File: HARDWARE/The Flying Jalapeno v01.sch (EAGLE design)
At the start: 94 parts, among them J2 7V, Q1 16MHZ, Q3 P-Channel MOSFET, Q5 MOSFET-PCHANNELNDP6020P_20V_2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, Q6 200mA/50V, Q7 200mA/50V, U4 ATMEGA2560AU

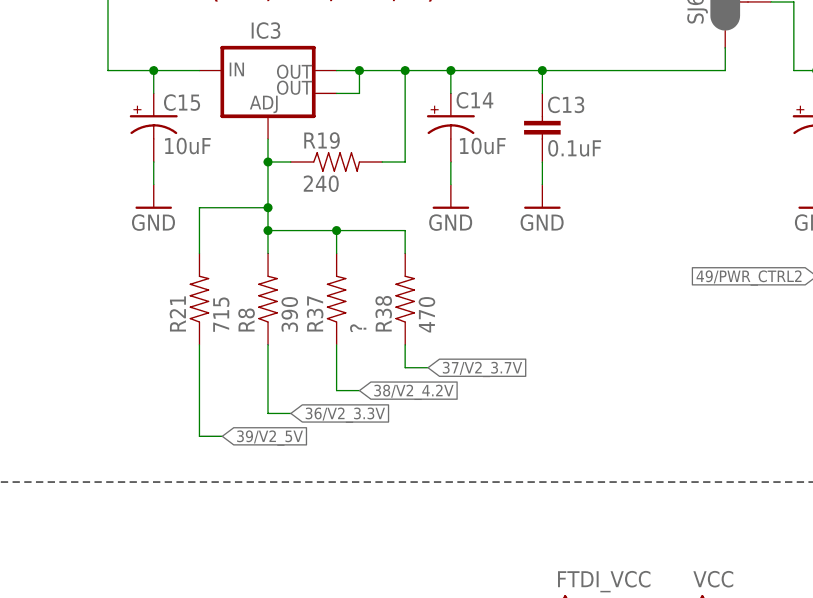
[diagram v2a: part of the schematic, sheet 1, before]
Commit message: finalized resistor values on lipo fake out vreg
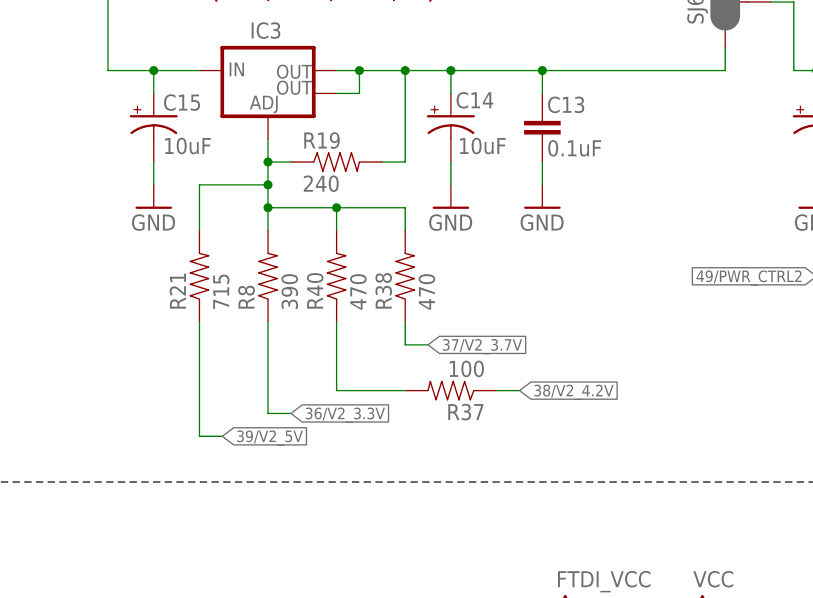
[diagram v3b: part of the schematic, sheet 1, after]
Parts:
- added R40: 470, SparkFun-Resistors:470OHM1/10W1%(0603)
- R37: value ? -> 100; device SparkFun-Resistors:390OHM1/10W1%(0603) -> SparkFun-Resistors:100OHM-1/10W-1%(0603)
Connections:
- new net N$1: R37.2, R40.1
- net N$10: now also R40.2; no longer R37.2
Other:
- moved on the sheet: R21, R37, R38, R8
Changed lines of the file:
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@@
 <part name="R36" library="SparkFun-Resistors" deviceset="10KOHM-1/10W-1%(0603)" device="0603" value="10K"/>
 <part name="GND38" library="SparkFun" deviceset="GND" device=""/>
-<part name="R37" library="SparkFun-Resistors" deviceset="390OHM1/10W1%(0603)" device="" value="?"/>
+<part name="R37" library="SparkFun-Resistors" deviceset="100OHM-1/10W-1%(0603)" device="" value="100"/>
 <part name="R38" library="SparkFun-Resistors" deviceset="470OHM1/10W1%(0603)" device="" value="470"/>
 <part name="R39" library="SparkFun-Resistors" deviceset="100KOHM-1/10W-1%(0603)" device="" value="100k"/>
@@
 <part name="R34" library="SparkFun-Resistors" deviceset="10KOHM-1/10W-1%(0603)" device="0603" value="10K"/>
 <part name="R35" library="SparkFun-Resistors" deviceset="10KOHM-1/10W-1%(0603)" device="0603" value="10K"/>
+<part name="R40" library="SparkFun-Resistors" deviceset="470OHM1/10W1%(0603)" device="" value="470"/>
 </parts>
 <sheets>
@@
 <attribute name="VALUE" x="71.12" y="121.92" size="1.778" layer="96"/>
 </instance>
-<instance part="R8" gate="G$1" x="68.58" y="106.68" rot="R90"/>
+<instance part="R8" gate="G$1" x="68.58" y="109.22" rot="R90"/>
 <instance part="R19" gate="G$1" x="76.2" y="121.92"/>
 <instance part="GND30" gate="1" x="99.06" y="116.84"/>
@@
 <attribute name="VALUE" x="165.608" y="122.174" size="1.778" layer="96" rot="R90"/>
 </instance>
-<instance part="R21" gate="G$1" x="60.96" y="106.68" rot="R90"/>
+<instance part="R21" gate="G$1" x="60.96" y="109.22" rot="R90"/>
 <instance part="SJ5" gate="G$1" x="114.3" y="203.2" smashed="yes" rot="MR0">
 <attribute name="NAME" x="110.109" y="200.66" size="1.778" layer="95" rot="MR90"/>
@@
 <instance part="R36" gate="G$1" x="149.86" y="246.38" rot="R90"/>
 <instance part="GND38" gate="1" x="149.86" y="236.22"/>
-<instance part="R37" gate="G$1" x="76.2" y="106.68" rot="R90"/>
-<instance part="R38" gate="G$1" x="83.82" y="106.68" rot="R90"/>
+<instance part="R37" gate="G$1" x="88.9" y="96.52" rot="R180"/>
+<instance part="R38" gate="G$1" x="83.82" y="109.22" rot="R90"/>
 <instance part="GND47" gate="1" x="68.58" y="38.1"/>
 <instance part="JP15" gate="G$1" x="60.96" y="50.8" rot="MR180"/>
@@
 <instance part="R34" gate="G$1" x="137.16" y="53.34" rot="R90"/>
 <instance part="R35" gate="G$1" x="152.4" y="53.34" rot="R90"/>
+<instance part="R40" gate="G$1" x="76.2" y="109.22" rot="R90"/>
 </instances>
 <busses>
@@
 <junction x="68.58" y="121.92"/>
 <pinref part="R21" gate="G$1" pin="2"/>
-<wire x1="60.96" y1="111.76" x2="60.96" y2="116.84" width="0.1524" layer="91"/>
-<wire x1="60.96" y1="116.84" x2="68.58" y2="116.84" width="0.1524" layer="91"/>
-<wire x1="68.58" y1="116.84" x2="68.58" y2="121.92" width="0.1524" layer="91"/>
+<wire x1="60.96" y1="114.3" x2="60.96" y2="119.38" width="0.1524" layer="91"/>
+<wire x1="60.96" y1="119.38" x2="68.58" y2="119.38" width="0.1524" layer="91"/>
+<wire x1="68.58" y1="119.38" x2="68.58" y2="121.92" width="0.1524" layer="91"/>
 <pinref part="R8" gate="G$1" pin="2"/>
-<wire x1="68.58" y1="111.76" x2="68.58" y2="114.3" width="0.1524" layer="91"/>
+<wire x1="68.58" y1="114.3" x2="68.58" y2="116.84" width="0.1524" layer="91"/>
+<junction x="68.58" y="119.38"/>
+<wire x1="68.58" y1="116.84" x2="68.58" y2="119.38" width="0.1524" layer="91"/>
 <junction x="68.58" y="116.84"/>
-<wire x1="68.58" y1="114.3" x2="68.58" y2="116.84" width="0.1524" layer="91"/>
-<wire x1="68.58" y1="114.3" x2="76.2" y2="114.3" width="0.1524" layer="91"/>
-<junction x="68.58" y="114.3"/>
 <pinref part="R38" gate="G$1" pin="2"/>
-<wire x1="76.2" y1="114.3" x2="83.82" y2="114.3" width="0.1524" layer="91"/>
-<wire x1="83.82" y1="114.3" x2="83.82" y2="111.76" width="0.1524" layer="91"/>
-<pinref part="R37" gate="G$1" pin="2"/>
-<wire x1="76.2" y1="111.76" x2="76.2" y2="114.3" width="0.1524" layer="91"/>
-<junction x="76.2" y="114.3"/>
+<wire x1="68.58" y1="116.84" x2="76.2" y2="116.84" width="0.1524" layer="91"/>
+<wire x1="76.2" y1="116.84" x2="83.82" y2="116.84" width="0.1524" layer="91"/>
+<wire x1="83.82" y1="116.84" x2="83.82" y2="114.3" width="0.1524" layer="91"/>
+<pinref part="R40" gate="G$1" pin="2"/>
+<wire x1="76.2" y1="114.3" x2="76.2" y2="116.84" width="0.1524" layer="91"/>
+<junction x="76.2" y="116.84"/>
 </segment>
 </net>
@@
 <segment>
 <pinref part="R38" gate="G$1" pin="1"/>
-<wire x1="83.82" y1="101.6" x2="83.82" y2="99.06" width="0.1524" layer="91"/>
-<wire x1="83.82" y1="99.06" x2="86.36" y2="99.06" width="0.1524" layer="91"/>
-<label x="86.36" y="99.06" size="1.27" layer="95" xref="yes"/>
+<wire x1="83.82" y1="104.14" x2="83.82" y2="101.6" width="0.1524" layer="91"/>
+<wire x1="83.82" y1="101.6" x2="86.36" y2="101.6" width="0.1524" layer="91"/>
+<label x="86.36" y="101.6" size="1.27" layer="95" xref="yes"/>
 </segment>
 <segment>
@@
 <segment>
 <pinref part="R37" gate="G$1" pin="1"/>
-<wire x1="76.2" y1="101.6" x2="76.2" y2="96.52" width="0.1524" layer="91"/>
-<wire x1="76.2" y1="96.52" x2="78.74" y2="96.52" width="0.1524" layer="91"/>
-<label x="78.74" y="96.52" size="1.27" layer="95" xref="yes"/>
+<wire x1="93.98" y1="96.52" x2="96.52" y2="96.52" width="0.1524" layer="91"/>
+<label x="96.52" y="96.52" size="1.27" layer="95" xref="yes"/>
 </segment>
 <segment>
@@
 <segment>
 <pinref part="R8" gate="G$1" pin="1"/>
-<wire x1="68.58" y1="101.6" x2="68.58" y2="93.98" width="0.1524" layer="91"/>
+<wire x1="68.58" y1="104.14" x2="68.58" y2="93.98" width="0.1524" layer="91"/>
 <wire x1="68.58" y1="93.98" x2="71.12" y2="93.98" width="0.1524" layer="91"/>
 <label x="71.12" y="93.98" size="1.27" layer="95" xref="yes"/>
@@
 <segment>
 <pinref part="R21" gate="G$1" pin="1"/>
-<wire x1="60.96" y1="101.6" x2="60.96" y2="91.44" width="0.1524" layer="91"/>
+<wire x1="60.96" y1="104.14" x2="60.96" y2="91.44" width="0.1524" layer="91"/>
 <wire x1="60.96" y1="91.44" x2="63.5" y2="91.44" width="0.1524" layer="91"/>
 <label x="63.5" y="91.44" size="1.27" layer="95" xref="yes"/>
@@
 </segment>
 </net>
+<net name="N$1" class="0">
+<segment>
+<pinref part="R40" gate="G$1" pin="1"/>
+<wire x1="76.2" y1="104.14" x2="76.2" y2="96.52" width="0.1524" layer="91"/>
+<pinref part="R37" gate="G$1" pin="2"/>
+<wire x1="76.2" y1="96.52" x2="83.82" y2="96.52" width="0.1524" layer="91"/>
+</segment>
+</net>

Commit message: Added labels to 2x30 connector
also a lot of other small stuff as I went through the checklist
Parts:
- removed IC3: (no value), SparkFun-PowerIC:V_REG_LM1117SOT223
- removed JP15: FTDI, SparkFun:ARDUINO_SERIAL_PROGRAMSMD
- removed JP6: FLYING_JALAPENO_V2FEMALE, SparkFun:FLYING_JALAPENO_V2FEMALE
- added JP2: FTDI, SparkFun:ARDUINO_SERIAL_PROGRAMSMD
- added JP4: 2x30 RA FEMALE HEADER, Testing:FLYING_JALAPENO_V2FEMALE
- added LOGO2: SFE_LOGO_FLAME.3_INCH, SparkFun-Aesthetics:SFE_LOGO_FLAME.3_INCH
- added U1: ATMEGA2560AU, SparkFun-DigitalIC:ATMEGA2560AU
- Q2, Q4: value (none) -> MMBT2222A
- Q3: value P-Channel MOSFET -> NDP6020P
- Q5: value MOSFET-PCHANNELNDP6020P_20V_24A_LOW_VGS_TH -> NDP6020P
- Q6, Q7: value 200mA/50V -> BSS138, 200mA/50V
- U2, U3: value (none) -> LM1117
- U4: value ATMEGA2560AU -> LM1117; device SparkFun:ATMEGA2560AU -> SparkFun-PowerIC:V_REG_LM1117SOT223
- renumbered IC1 to U2, IC2 to U3, J2 to JP1, Q1 to Y1, SJ5 to SJ3, SJ6 to SJ4
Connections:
- net 31/CAPRETURN2: now also U1.(A14)PC6; no longer U4.(A14)PC6
- net 33/V1_3.3V: now also U1.(A12)PC4; no longer U4.(A12)PC4
- net 34/RAW_PASS_LED: now also U1.(A11)PC3; no longer U4.(A11)PC3
- net 35/V1_5V: now also U1.(A10)PC2; no longer U4.(A10)PC2
- net 36/V2_3.3V: now also U1.(A9)PC1; no longer U4.(A9)PC1
- net 37/V2_3.7V: now also U1.(A8)PC0; no longer U4.(A8)PC0
- net 38/V2_4.2V: now also U1.(T0)PD7; no longer U4.(T0)PD7
- net 39/V2_5V: now also U1.(ALE)PG2; no longer U4.(ALE)PG2
- net 40/FAIL: now also U1.(RD)PG1; no longer U4.(RD)PG1
- net 41/PASS: now also U1.(WR)PG0; no longer U4.(WR)PG0
- net 42/PT_FAIL: now also U1.PL7; no longer U4.PL7
- net 43/PT_PASS: now also U1.PL6; no longer U4.PL6
- net 44/PT_CTRL: now also U1.PL5(OC5C); no longer U4.PL5(OC5C)
- net 45/CAPSENSE1: now also JP4.CAP_PAD1, U1.PL4(OC5B); no longer JP6.CAP_PAD1, U4.PL4(OC5B)
- net 46/CAPSENSE2: now also JP4.CAP_PAD2, U1.PL3(OC5A); no longer JP6.CAP_PAD2, U4.PL3(OC5A)
- net 47/CAPRETURN1: now also U1.PL2(T5); no longer U4.PL2(T5)
- net 48/PWR_CTRL1: now also U1.PL1(ICP5); no longer U4.PL1(ICP5)
- net 49/PWR_CTRL2: now also U1.PL0(ICP4); no longer U4.PL0(ICP4)
- net A0: now also JP4.A0(RX0), U1.(ADC0)PF0; no longer JP6.A0(RX0), U4.(ADC0)PF0
- net A1: now also JP4.A1(TX0), U1.(ADC1)PF1; no longer JP6.A1(TX0), U4.(ADC1)PF1
- net A10: now also JP4.A10, U1.PK2(ADC10/PCINT18); no longer JP6.A10, U4.PK2(ADC10/PCINT18)
- net A11: now also JP4.A11, U1.PK3(ADC11/PCINT19); no longer JP6.A11, U4.PK3(ADC11/PCINT19)
- net A12: now also JP4.A12, U1.PK4(ADC12/PCINT20); no longer JP6.A12, U4.PK4(ADC12/PCINT20)
- net A13/RAW_READ: now also U1.PK5(ADC13/PCINT21); no longer U4.PK5(ADC13/PCINT21)
- net A14/PT_READ_V1: now also U1.PK6(ADC14/PCINT22); no longer U4.PK6(ADC14/PCINT22)
- net A15/PT_READ_V2: now also U1.PK7(ADC15/PCINT23); no longer U4.PK7(ADC15/PCINT23)
- net A2: now also JP4.A2, U1.(ADC2)PF2; no longer JP6.A2, U4.(ADC2)PF2
- net A3: now also JP4.A3, U1.(ADC3)PF3; no longer JP6.A3, U4.(ADC3)PF3
- net A4: now also JP4.A4, U1.(ADC4/TCK)PF4; no longer JP6.A4, U4.(ADC4/TCK)PF4
- net A5: now also JP4.A5, U1.(ADC5/TMS)PF5; no longer JP6.A5, U4.(ADC5/TMS)PF5
- net A6: now also JP4.A6, U1.(ADC6/TDO)PF6; no longer JP6.A6, U4.(ADC6/TDO)PF6
- net A7: now also JP4.A7, U1.(ADC7/TDI)PF7; no longer JP6.A7, U4.(ADC7/TDI)PF7
- net A8: now also JP4.A8, U1.PK0(ADC8/PCINT16); no longer JP6.A8, U4.PK0(ADC8/PCINT16)
- net A9: now also JP4.A9, U1.PK1(ADC9/PCINT17); no longer JP6.A9, U4.PK1(ADC9/PCINT17)
- net AREF: now also U1.AREF; no longer U4.AREF
- net D10: now also JP4.10, U1.(OC2A/PCINT4)PB4; no longer JP6.10, U4.(OC2A/PCINT4)PB4
- net D11: now also JP4.11, U1.(OC1A/PCINT5)PB5; no longer JP6.11, U4.(OC1A/PCINT5)PB5
- net D12: now also JP4.12, U1.(OC1B/PCINT6)PB6; no longer JP6.12, U4.(OC1B/PCINT6)PB6
- net D13: now also JP4.13, U1.(OC0A/OC1C/PCINT7)PB7; no longer JP6.13, U4.(OC0A/OC1C/PCINT7)PB7
- net D2: now also JP4.2(INT0), U1.(OC3B/INT4)PE4; no longer JP6.2(INT0), U4.(OC3B/INT4)PE4
- net D22: now also JP4.22, U1.(AD0)PA0; no longer JP6.22, U4.(AD0)PA0
- net D23: now also JP4.23, U1.(AD1)PA1; no longer JP6.23, U4.(AD1)PA1
- net D24: now also JP4.24, U1.(AD2)PA2; no longer JP6.24, U4.(AD2)PA2
- net D25: now also JP4.25, U1.(AD3)PA3; no longer JP6.25, U4.(AD3)PA3
- net D26: now also JP4.26, U1.(AD4)PA4; no longer JP6.26, U4.(AD4)PA4
- net D27: now also JP4.27, U1.(AD5)PA5; no longer JP6.27, U4.(AD5)PA5
- net D28: now also JP4.28, U1.(AD6)PA6; no longer JP6.28, U4.(AD6)PA6
- net D29: now also JP4.29, U1.(AD7)PA7; no longer JP6.29, U4.(AD7)PA7
- net D3: now also JP4.3(INT1), U1.(OC3C/INT5)PE5; no longer JP6.3(INT1), U4.(OC3C/INT5)PE5
- net D30: now also JP4.30, U1.(A15)PC7; no longer JP6.30, U4.(A15)PC7
- net D4: now also JP4.4, U1.(OC0B)PG5; no longer JP6.4, U4.(OC0B)PG5
- net D5: now also JP4.5, U1.(OC3A/AIN1)PE3; no longer JP6.5, U4.(OC3A/AIN1)PE3
- net D6: now also JP4.6, U1.PH3(OC4A); no longer JP6.6, U4.PH3(OC4A)
- net D7: now also JP4.7, U1.PH4(OC4B); no longer JP6.7, U4.PH4(OC4B)
- net D8: now also JP4.8, U1.PH5(OC4C); no longer JP6.8, U4.PH5(OC4C)
- net D9: now also JP4.9, U1.PH6(OC2B); no longer JP6.9, U4.PH6(OC2B)
- net DTR: now also JP2.DTR; no longer JP15.DTR
- net FTDI_VCC: now also JP2.VCC; no longer JP15.VCC
- net GND: now also JP2.CTS, JP2.GND, JP4.GND, U1.AGND, U1.GND, U1.GND1, U1.GND2, U1.GND3; no longer JP15.CTS, JP15.GND, JP6.GND, U4.AGND, U4.GND, U4.GND1, U4.GND2, U4.GND3
- net N$10: now also U4.ADJ; no longer IC3.ADJ
- net N$16: now also JP2.TXO; no longer JP15.TXO
- net N$19: now also JP4.41/PASS; no longer JP6.41/PASS
- net N$20: now also JP4.40/FAIL; no longer JP6.40/FAIL
- net N$26: now also JP2.RXI; no longer JP15.RXI
- net N$6: now also JP4.43/PT_PASS; no longer JP6.43/PT_PASS
- net N$7: now also JP4.42/PT_FAIL; no longer JP6.42/PT_FAIL
- net N$73: now also U1.XTAL2; no longer U4.XTAL2
- net N$74: now also U1.XTAL1; no longer U4.XTAL1
- net PB0: now also JP4.53, U1.(SS/PCINT0)PB0; no longer JP6.53, U4.(SS/PCINT0)PB0
- net PB1: now also JP4.52, U1.(SCK/PCINT1)PB1; no longer JP6.52, U4.(SCK/PCINT1)PB1
- net PB2: now also JP4.51, U1.(MOSI/PCINT2)PB2; no longer JP6.51, U4.(MOSI/PCINT2)PB2
- net PB3: now also JP4.50, U1.(MISO/PCINT3)PB3; no longer JP6.50, U4.(MISO/PCINT3)PB3
- net PC5: now also U1.(A13)PC5; no longer U4.(A13)PC5
- net RAW: now also JP4.RAW, U4.IN; no longer IC3.IN, JP6.RAW
- net RESET: now also U1.RESET; no longer U4.RESET
- net RX0: now also U1.(RXD0/PCIN8)PE0; no longer U4.(RXD0/PCIN8)PE0
- net RX1: now also JP4.19(RX1/INT4), U1.(RXD1/INT2)PD2; no longer JP6.19(RX1/INT4), U4.(RXD1/INT2)PD2
- net RX2: now also JP4.17(RX2), U1.PH0(RXD2); no longer JP6.17(RX2), U4.PH0(RXD2)
- net RX3: now also JP4.15(RX3), U1.PJ0(RXD3/PCINT9); no longer JP6.15(RX3), U4.PJ0(RXD3/PCINT9)
- net SCL: now also JP4.21(SCL/INT2), U1.(SCL/INT0)PD0; no longer JP6.21(SCL/INT2), U4.(SCL/INT0)PD0
- net SDA: now also JP4.20(SDA/INT3), U1.(SDA/INT1)PD1; no longer JP6.20(SDA/INT3), U4.(SDA/INT1)PD1
- net TX0: now also U1.(TXD0)PE1; no longer U4.(TXD0)PE1
- net TX1: now also JP4.18(TX1/INT5), U1.(TXD1/INT3)PD3; no longer JP6.18(TX1/INT5), U4.(TXD1/INT3)PD3
- net TX2: now also JP4.16(TX2), U1.PH1(TXD2); no longer JP6.16(TX2), U4.PH1(TXD2)
- net TX3: now also JP4.14(TX3), U1.PJ1(TXD3/PCINT10); no longer JP6.14(TX3), U4.PJ1(TXD3/PCINT10)
- net V1: now also JP4.V1; no longer JP6.V1
- net V2: now also JP4.V2; no longer JP6.V2
- net VCC: now also U1.AVCC, U1.VCC, U1.VCC1, U1.VCC2, U1.VCC3; no longer U4.AVCC, U4.VCC, U4.VCC1, U4.VCC2, U4.VCC3
- net VREG2OUT: now also U4.OUT, U4.OUT@1; no longer IC3.OUT, IC3.OUT@1
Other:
- note added: "->3.3V"
- note added: "2x30 RA connector to testbeds"
- note added: "5V<-"
- note added: "INPUT VOLTAGE 7-16V Varies depending on testbed"
